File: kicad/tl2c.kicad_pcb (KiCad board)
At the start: 2 copper layers, 78 parts, among them IC101 ATTINY20-X, P101 12VDC, P102 I2C Master, P103 Spare, P104 ISP Header, P105 LED_DRIVER, P106 240VAC, P107 LED_DRIVER, P108 LED_OUT, P301 PIR13, Q301 IRLML2502, Q302 IRLML2502, Q303 IRLML2502, Q401 IRLML2502, Q402 IRLML2502, Q403 IRLML2502, SW101 TL3315NF160Q, U201 LF120ABDT-TR, U202 TPS70933

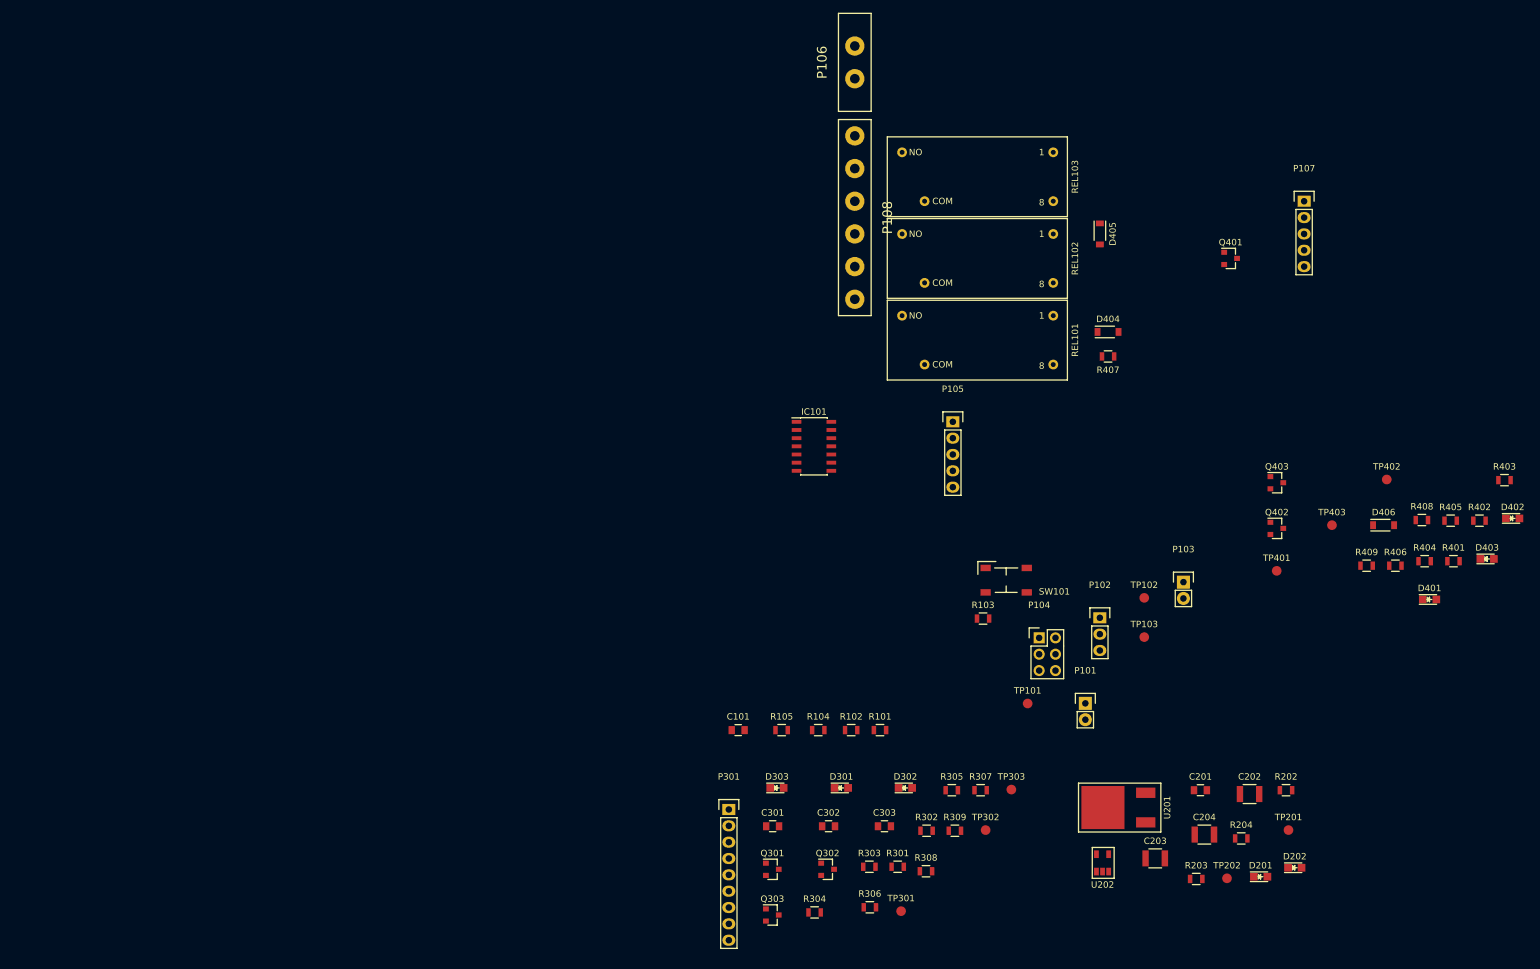
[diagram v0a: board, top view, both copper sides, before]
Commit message: Started adding tracks to the layout
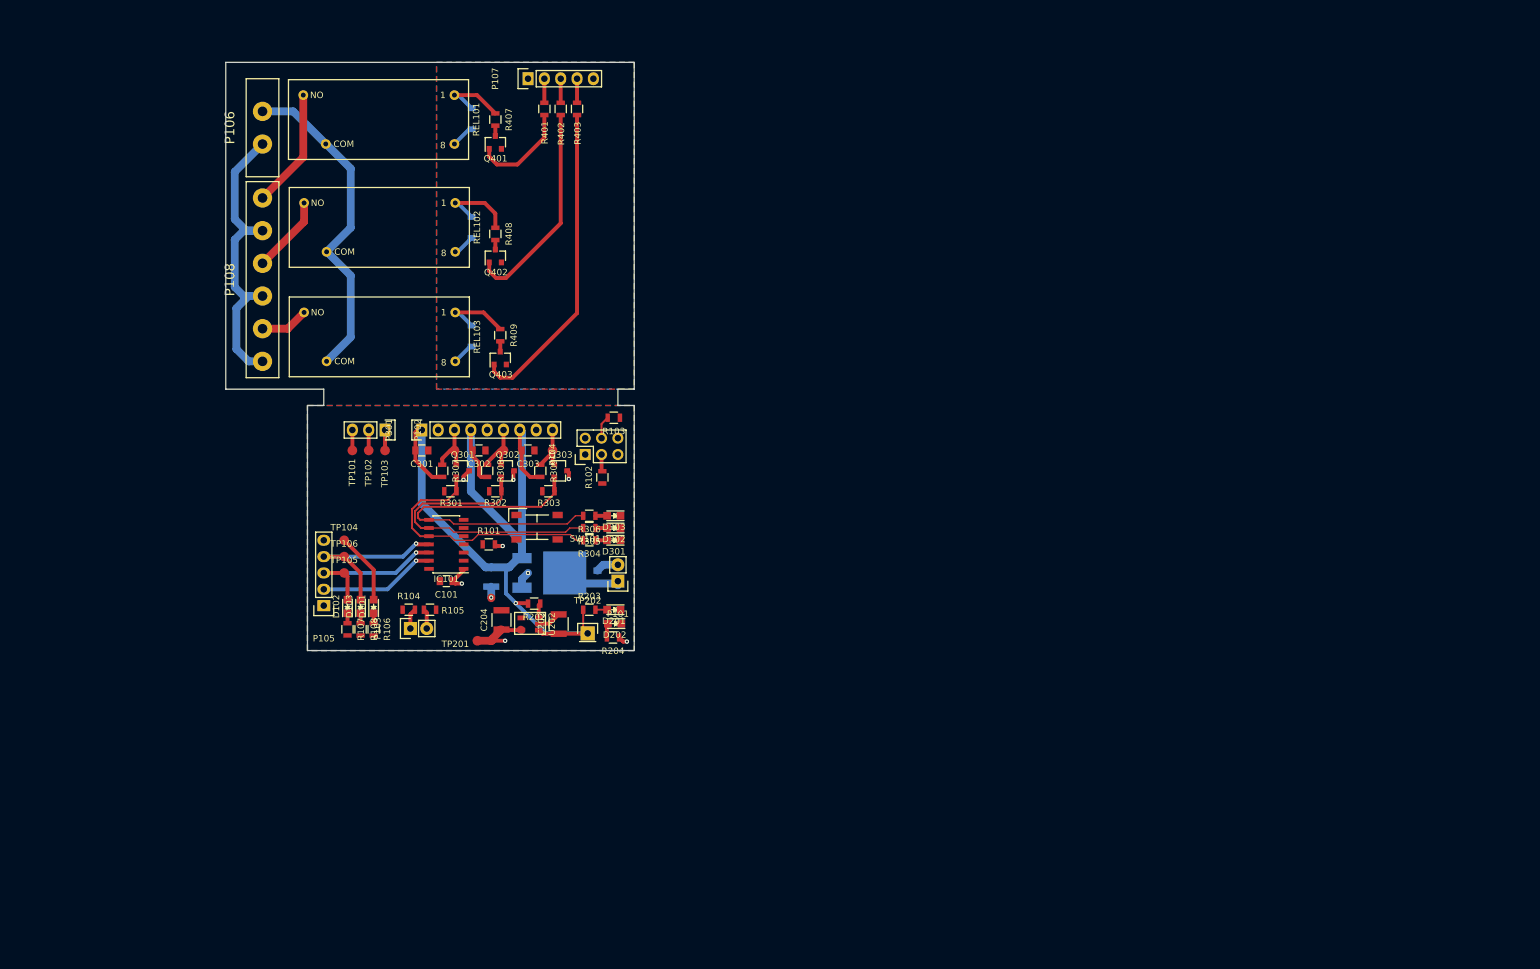
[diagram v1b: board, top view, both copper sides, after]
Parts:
- removed D401: LED_UG, LEDs:LED_0805
- removed D402: LED_EG, LEDs:LED_0805
- removed D403: LED_OG, LEDs:LED_0805
- removed R404, R405, R406: 660Ω, Resistors_SMD:R_0805
- removed TP401: TP_RLY_UG, Measurement_Points:Measurement_Point_Round-SMD-Pad_Small
- removed TP402: TP_RLY_EG, Measurement_Points:Measurement_Point_Round-SMD-Pad_Small
- removed TP403: TP_RLY_OG, Measurement_Points:Measurement_Point_Round-SMD-Pad_Small
- added D101: LED_UG, LEDs:LED_0805, F.Cu at (104.3, 110.0)
- added D102: LED_EG, LEDs:LED_0805, F.Cu at (100.2, 110.0)
- added D103: LED_OG, LEDs:LED_0805, F.Cu at (102.2, 110.0)
- added R106: 660Ω, Resistors_SMD:R_0805, F.Cu at (104.3, 113.5)
- added R107: 660Ω, Resistors_SMD:R_0805, F.Cu at (100.2, 113.5)
- added R108: 660Ω, Resistors_SMD:R_0805, F.Cu at (102.2, 113.5)
- added TP104: TP_RLY_UG, Measurement_Points:Measurement_Point_Round-SMD-Pad_Small, F.Cu at (99.7, 99.7)
- added TP105: TP_RLY_EG, Measurement_Points:Measurement_Point_Round-SMD-Pad_Small, F.Cu at (99.7, 104.8)
- added TP106: TP_RLY_OG, Measurement_Points:Measurement_Point_Round-SMD-Pad_Small, F.Cu at (99.7, 102.2)
- C201, C203, D404, D405, D406, U201: moved to B.Cu
- TP202: footprint Measurement_Points:Measurement_Point_Round-SMD-Pad_Small -> Pin_Headers:Pin_Header_Straight_1x01
- moved R401 157.8 mm to (130.8, 32.6), turned to 90 degrees
- moved R402 156.5 mm to (133.3, 32.6), turned to 90 degrees
- moved R403 155.3 mm to (135.9, 32.6), turned to 90 degrees
- moved R408 150.7 mm to (123.2, 52.1), turned to 270 degrees
- moved D406 144.8 mm to (119.5, 67.9), turned to 90 degrees
- moved R409 139.4 mm to (124.0, 67.8), turned to 270 degrees
- moved TP201 129.5 mm to (120.4, 115.3), turned to 180 degrees
- moved Q402 128.7 mm to (123.2, 55.5), turned to 90 degrees
- moved TP102 122.7 mm to (103.5, 85.7), turned to 270 degrees
- moved Q403 122.3 mm to (124.0, 71.4), turned to 90 degrees
- moved P107 122.1 mm to (128.3, 27.9), turned to 90 degrees
- moved TP103 121.5 mm to (106.0, 85.7), turned to 270 degrees
- moved R202 120.4 mm to (129.2, 109.5), turned to 180 degrees
- moved P103 120.4 mm to (110.0, 113.4), turned to 90 degrees
- moved Q401 115.7 mm to (123.2, 37.8), turned to 90 degrees
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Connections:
- C101 pad 1: /PIR13/InUb+ -> /PIR13/Ub+
- C202 pad 1: /PIR13/InU+ -> /PIR13/U+
- C203 pad 1: /PIR13/InU+ -> /PIR13/U+
- C204 pad 1: /PIR13/InUb+ -> /PIR13/Ub+
- C301 pad 2: /PIR13/InU+ -> /PIR13/U+
- C302 pad 2: /PIR13/InU+ -> /PIR13/U+
- C303 pad 2: /PIR13/InU+ -> /PIR13/U+
- D201 pad 1: Net-(D201-Pad1) -> GND
- D201 pad 2: /PIR13/InU+ -> Net-(D201-Pad2)
- D202 pad 1: Net-(D202-Pad1) -> GND
- D202 pad 2: /PIR13/InUb+ -> Net-(D202-Pad2)
- D301 pad 1: Net-(D301-Pad1) -> GND
- D301 pad 2: /PIR13/SIG_UG -> Net-(D301-Pad2)
- D302 pad 1: Net-(D302-Pad1) -> GND
- D302 pad 2: /PIR13/SIG_EG -> Net-(D302-Pad2)
- D303 pad 1: Net-(D303-Pad1) -> GND
- D303 pad 2: /PIR13/SIG_OG -> Net-(D303-Pad2)
- D404 pad 1: /PIR13/InU+ -> /LED Driver/LED_DRIVER_U+
- D405 pad 1: /PIR13/InU+ -> /LED Driver/LED_DRIVER_U+
- D406 pad 1: /PIR13/InU+ -> /LED Driver/LED_DRIVER_U+
- IC101 pad 1: /PIR13/InUb+ -> /PIR13/Ub+
- P104 pad 2: /PIR13/InUb+ -> /PIR13/Ub+
- P105 pad 1: /PIR13/InUb+ -> /PIR13/Ub+
- P107 pad 1: /PIR13/InU+ -> /LED Driver/LED_DRIVER_U+
- P107 pad 2: /LED Driver/Relay_OG -> /LED Driver/Relay_UG
- P107 pad 4: /LED Driver/Relay_UG -> /LED Driver/Relay_OG
- P107 pad 5: GND -> GNDA
- P301 pad 1: /PIR13/InU+ -> /PIR13/U+
- P301 pad 4: /PIR13/InU+ -> /PIR13/U+
- P301 pad 7: /PIR13/InU+ -> /PIR13/U+
- Q301 pad 3: /PIR13/InUb+ -> /PIR13/Ub+
- Q302 pad 3: /PIR13/InUb+ -> /PIR13/Ub+
- Q303 pad 3: /PIR13/InUb+ -> /PIR13/Ub+
- Q401 pad 2: GND -> GNDA
- Q402 pad 2: GND -> GNDA
- Q403 pad 2: GND -> GNDA
- R101 pad 2: /PIR13/InUb+ -> /PIR13/Ub+
- R202 pad 2: /PIR13/InU+ -> /PIR13/U+
- R203 pad 1: Net-(D201-Pad1) -> /PIR13/U+
- R203 pad 2: GND -> Net-(D201-Pad2)
- R204 pad 1: Net-(D202-Pad1) -> /PIR13/Ub+
- R204 pad 2: GND -> Net-(D202-Pad2)
- R304 pad 1: GND -> Net-(D301-Pad2)
- R304 pad 2: Net-(D301-Pad1) -> /PIR13/SIG_UG
- R305 pad 1: GND -> Net-(D302-Pad2)
- R305 pad 2: Net-(D302-Pad1) -> /PIR13/SIG_EG
- R306 pad 1: GND -> Net-(D303-Pad2)
- R306 pad 2: Net-(D303-Pad1) -> /PIR13/SIG_OG
- R307 pad 2: /PIR13/InU+ -> /PIR13/U+
- R308 pad 2: /PIR13/InU+ -> /PIR13/U+
- R309 pad 2: /PIR13/InU+ -> /PIR13/U+
- REL101 pad 8: /PIR13/InU+ -> /LED Driver/LED_DRIVER_U+
- REL102 pad 8: /PIR13/InU+ -> /LED Driver/LED_DRIVER_U+
- REL103 pad 8: /PIR13/InU+ -> /LED Driver/LED_DRIVER_U+
- SW101 pad 2: (no net) -> Net-(SW101-Pad2)
- SW101 pad 4: (no net) -> Net-(SW101-Pad4)
- TP201 pad 1: /PIR13/InUb+ -> /PIR13/Ub+
- TP202 pad 1: /PIR13/InU+ -> /PIR13/U+
- U201 pad 2: /PIR13/InU+ -> /PIR13/U+
- U202 pad 1: /PIR13/InU+ -> /PIR13/U+
- U202 pad 4: (no net) -> Net-(U202-Pad4)
- U202 pad 5: /PIR13/InUb+ -> /PIR13/Ub+
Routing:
- net /PIR13/U+: track 0.00 -> 137.6 mm, vias 0 -> 1
- net /PIR13/SIG_OG: track 0.00 -> 52.4 mm
- net /Lin: track 0.00 -> 51.9 mm
- net /Neutral: track 0.00 -> 51.7 mm
- net Net-(Q403-Pad1): track 0.00 -> 49.3 mm
- net /PIR13/SIG_EG: track 0.00 -> 46.4 mm
- net /PIR13/SIG_UG: track 0.00 -> 41.4 mm
- net Net-(Q402-Pad1): track 0.00 -> 33.3 mm
- net /RelayUG: track 0.00 -> 29.3 mm, vias 0 -> 1
- net /RelayOG: track 0.00 -> 28.4 mm, vias 0 -> 1
- net /RelayEG: track 0.00 -> 25.2 mm, vias 0 -> 1
- net /PIR13/Ub+: track 0.00 -> 21.9 mm, vias 0 -> 7
- net /LineUG: track 0.00 -> 18.6 mm
- net Net-(Q401-Pad1): track 0.00 -> 15.5 mm
- net GND: track 0.00 -> 14.9 mm, vias 0 -> 2
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- added copper zone on B.Cu, net /LED Driver/LED_DRIVER_U+
- added copper zone on B.Cu, net /PIR13/Ub+
- added copper zone on F.Cu, net GND
- added copper zone on F.Cu, net GNDA
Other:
- board outline added: 63.5 x 91.4 mm
- net class Default: clearance 0.2 -> 0.1524; trace_width 0.25 -> 0.1524; via_dia 0.6 -> 0.6858; via_drill 0.4 -> 0.3302
- rule trace_clearance: 0.2 -> 0.1524
- rule trace_min: 0.2 -> 0.1524
- rule via_min_drill: 0.3 -> 0.3302
- rule via_min_size: 0.4 -> 0.6858

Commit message: Retried the track layouts for the contoller part.
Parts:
- C101, C301, C302, C303, R104, R105, R106, R107, R108, R203, R204, R304, R305, R306: moved to B.Cu
- moved C101 8.25 mm to (115.6, 97.8), turned to 270 degrees
- moved TP104 7.62 mm to (99.7, 107.3)
- moved R301 5.12 mm to (111.8, 89.5)
- moved IC101 5.12 mm to (111.1, 97.8), turned to 270 degrees
- moved R306 4.58 mm to (141.6, 93.3)
- moved D103 4.51 mm to (106.0, 112.4)
- moved D101 4.09 mm to (101.0, 112.4)
- moved D102 4.09 mm to (103.5, 112.4)
- moved R302 4.07 mm to (120.0, 89.5)
- moved R307 4.07 mm to (111.8, 86.4), turned to 90 degrees
- moved R303 4.07 mm to (128.3, 89.5)
- moved R305 4.02 mm to (141.6, 96.5)
- moved R108 3.98 mm to (106.0, 112.4), turned to 90 degrees
- moved R203 3.81 mm to (141.6, 110.5)
- moved R304 3.81 mm to (141.6, 99.7)
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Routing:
- net /PIR13/U+: track 137.6 -> 0.00 mm, vias 1 -> 0
- net /PIR13/SIG_OG: track 52.4 -> 0.00 mm
- net /PIR13/SIG_EG: track 46.4 -> 0.00 mm
- net /PIR13/SIG_UG: track 41.4 -> 0.00 mm
- net /RelayUG: track 29.3 -> 0.00 mm, vias 1 -> 0
- net /RelayOG: track 28.4 -> 0.00 mm, vias 1 -> 0
- net /RelayEG: track 25.2 -> 0.00 mm, vias 1 -> 0
- net /PIR13/Ub+: track 21.9 -> 0.00 mm, vias 7 -> 0
- net GND: track 14.9 -> 0.00 mm, vias 2 -> 0
- net /Power System/U+In: track 9.68 -> 0.00 mm
- net /PIR13/PIR_OG: track 9.29 -> 0.00 mm
- net /PIR13/PIR_EG: track 9.20 -> 0.00 mm
- net /PIR13/PIR_UG: track 8.90 -> 0.00 mm
- net /MOSI: track 3.57 -> 0.00 mm
- net /Spare1: track 3.21 -> 0.00 mm
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
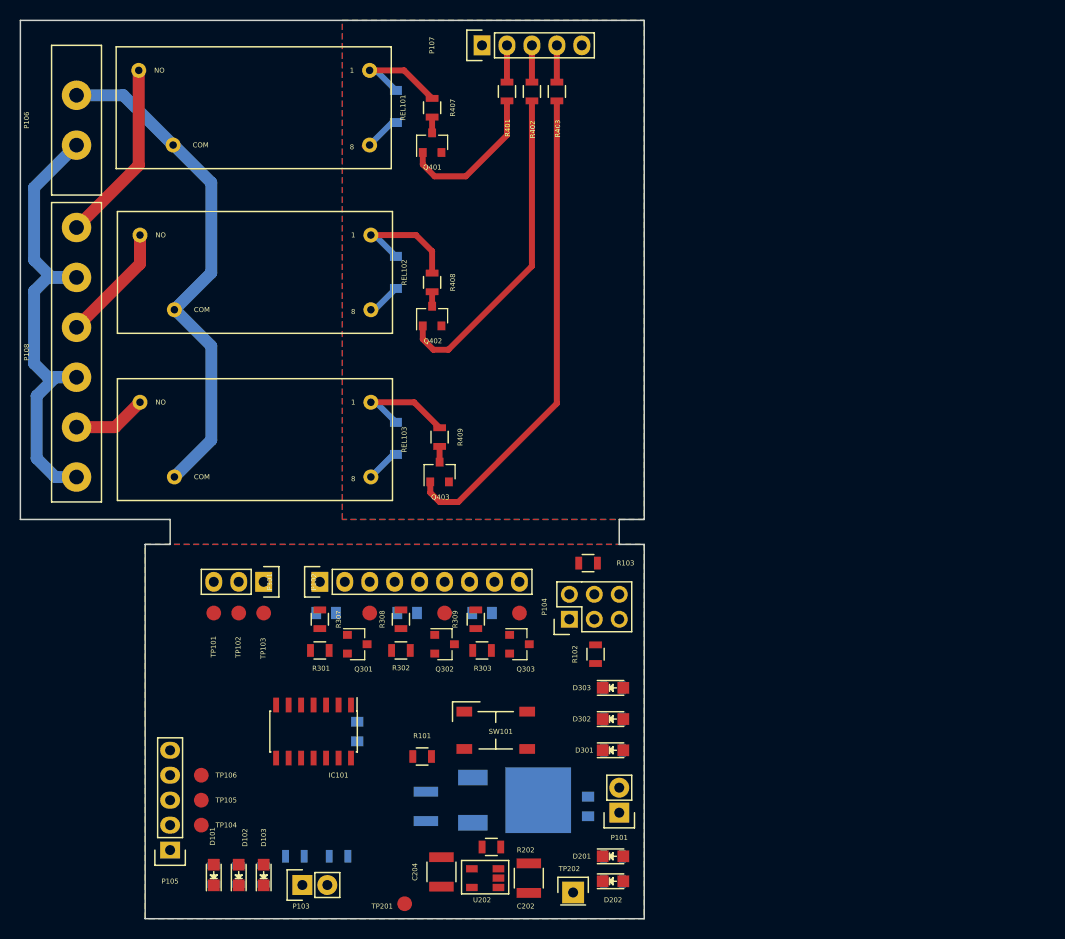
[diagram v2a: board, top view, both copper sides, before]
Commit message: Completed the first draft of the board - moved to 4 layers
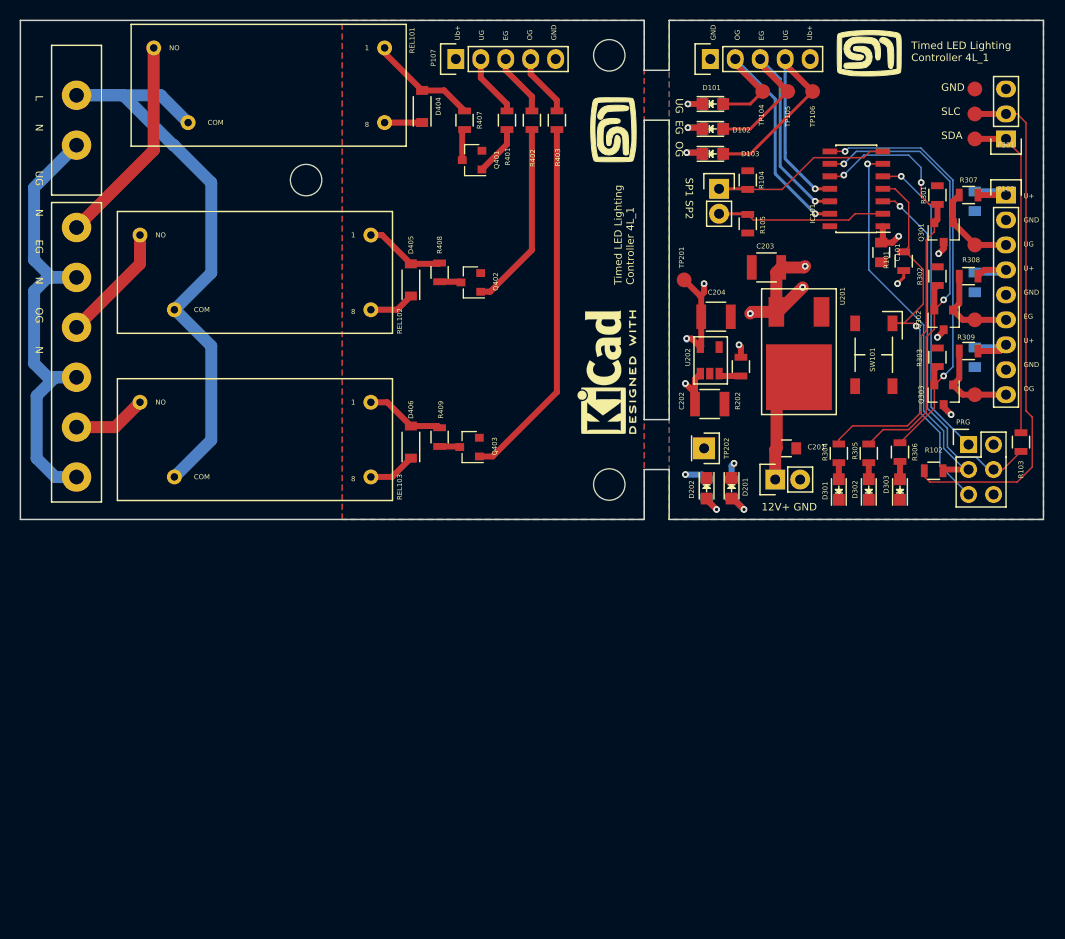
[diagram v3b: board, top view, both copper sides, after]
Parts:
- added G***: LOGO, tl2c-footprint:MyBasic_rounded_50_1, F.Cu at (141.6, 36.6)
- added G***: LOGO, tl2c-footprint:MyBasic_rounded_50_1, F.Cu at (167.6, 28.7)
- added REF**: MountingHole_3.2mm_M3, Mounting_Holes:MountingHole_3.2mm_M3, F.Cu at (141.2, 72.6)
- added REF**: MountingHole_3.2mm_M3, Mounting_Holes:MountingHole_3.2mm_M3, F.Cu at (141.2, 29.0)
- added REF**: MountingHole_3.2mm_M3, Mounting_Holes:MountingHole_3.2mm_M3, F.Cu at (110.4, 41.7)
- added REF***: KiCad-Logo2_6mm_SilkScreen, Symbols:KiCad-Logo2_6mm_SilkScreen, F.Cu at (141.0, 61.2)
- C101, C201, C203, D404, D405, D406, R104, R105, R304, R305, R306, U201: moved to F.Cu
- moved P105 97.5 mm to (151.5, 29.3), turned to 90 degrees
- moved TP101 94.1 mm to (178.4, 32.4), turned to 180 degrees
- moved TP104 94.0 mm to (156.8, 32.6), turned to 270 degrees
- moved TP105 93.6 mm to (159.4, 32.6), turned to 270 degrees
- moved D101 93.5 mm to (151.8, 33.9), turned to 0 degrees
- moved R106 93.5 mm to (151.8, 33.9), turned to 0 degrees
- moved TP106 93.4 mm to (161.9, 32.6), turned to 270 degrees
- moved TP102 90.5 mm to (178.4, 34.9), turned to 180 degrees
- moved D102 90.0 mm to (151.8, 36.4), turned to 0 degrees
- moved R107 90.0 mm to (151.8, 36.4), turned to 0 degrees
- moved P102 88.0 mm to (181.6, 37.5), turned to 180 degrees
- moved TP103 87.0 mm to (178.4, 37.5), turned to 180 degrees
- moved D103 86.5 mm to (151.8, 39.0), turned to 0 degrees
- moved R108 86.5 mm to (151.8, 39.0), turned to 0 degrees
- moved R104 82.8 mm to (155.3, 41.7), turned to 270 degrees
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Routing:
- net /SCL: track 0.00 -> 53.5 mm
- net /PIR13/SIG_EG: track 0.00 -> 48.3 mm, vias 0 -> 2
- net /PIR13/SIG_UG: track 0.00 -> 48.1 mm, vias 0 -> 2
- net /PIR13/SIG_OG: track 0.00 -> 45.0 mm, vias 0 -> 2
- net /PIR13/U+: track 0.00 -> 41.9 mm, vias 0 -> 6
- net /Reset: track 0.00 -> 41.5 mm, vias 0 -> 1
- net /SCK: track 0.00 -> 40.6 mm, vias 0 -> 1
- net /MOSI: track 0.00 -> 37.7 mm, vias 0 -> 1
- net /SDA: track 0.00 -> 33.7 mm
- net /RelayOG: track 0.00 -> 32.2 mm, vias 0 -> 1
- net /MISO: track 0.00 -> 32.0 mm, vias 0 -> 1
- net /RelayEG: track 0.00 -> 30.9 mm, vias 0 -> 1
- net /RelayUG: track 0.00 -> 29.6 mm, vias 0 -> 1
- net /PIR13/Ub+: track 0.00 -> 22.4 mm, vias 0 -> 8
- net /Spare1: track 0.00 -> 18.6 mm
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- added copper zone on U+, net /PIR13/U+
- added copper zone on Ub+, net /PIR13/Ub+
- added copper zone on B.Cu, net GND
- removed copper zone on B.Cu, net /PIR13/Ub+
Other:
- board size 63.5 x 91.4 mm -> 104.1 x 50.8 mm
- copper layers 2 -> 4
- board text added: "12V+ GND"
- board text added: "CUT OUT"
- board text added: "GND OG EG UG Ub+"
- board text added: "GND SLC SDA"
- board text added: "L N UG N EG N OG N"
- board text added: "PRG"
- board text added: "SP1 SP2"
- board text added: "Timed LED Lighting Controller 4L_1"
- board text added: "U+ GND UG U+ GND EG U+ GND OG"
- board text added: "UG EG OG"
- board text added: "Ub+ UG EG OG GND"
